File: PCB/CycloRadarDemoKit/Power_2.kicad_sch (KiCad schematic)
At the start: 16 parts, among them U401 AP63203WU, U404 TPS2121RUXR

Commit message: PCB, 3Dmodel
mockup PCB version done, schcematic exported to latex, 3D model generated and exported to latex
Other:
- title: Safety Ride Radar Sensor -> Radar Safety Sensor
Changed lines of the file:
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@@
   (paper "A4")
   (title_block
-    (title "Safety Ride Radar Sensor")
-    (date "2023-12-19")
-    (rev "Rev.: WIP")
+    (title "Radar Safety Sensor")
+    (date "2023-12-20")
+    (rev "Rev.: 1")
     (company "ALPS Electric Czech, s.r.o.")
     (comment 1 "Designed by Martin Tavoda")

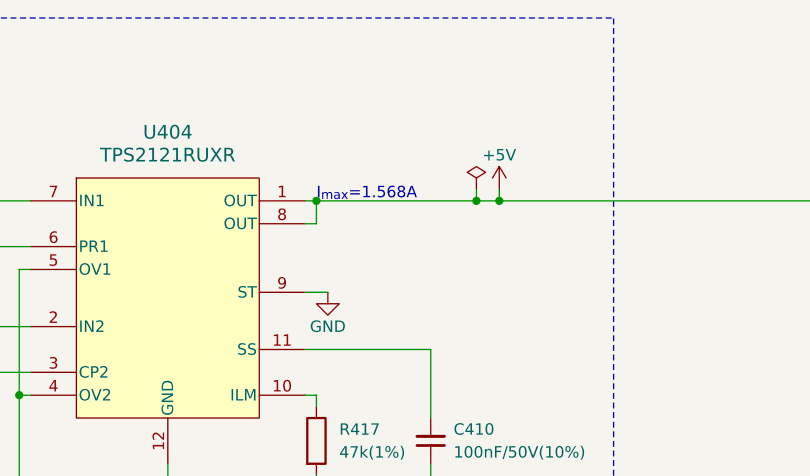
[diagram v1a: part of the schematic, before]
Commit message: sortingAbbr, cosmetics schematic, export schematic to thesis
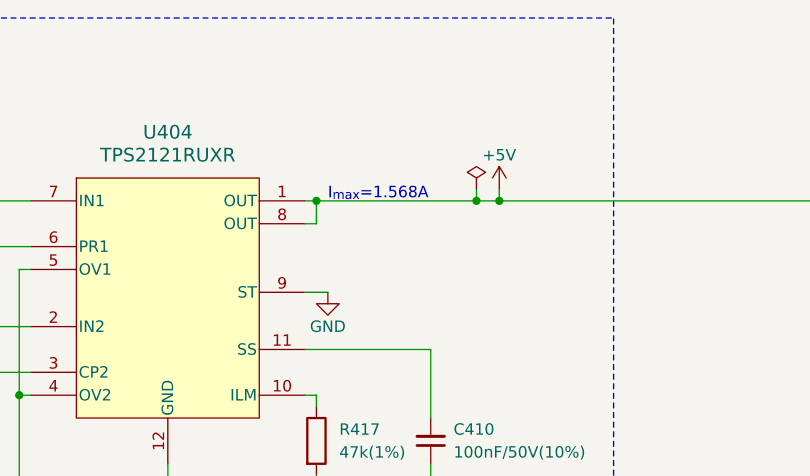
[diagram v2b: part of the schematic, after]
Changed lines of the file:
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@@
     (title "Radar Safety Sensor")
     (date "2023-12-20")
-    (rev "Rev.: 1")
+    (rev "Rev.: 1.0")
     (company "ALPS Electric Czech, s.r.o.")
     (comment 1 "Designed by Martin Tavoda")
@@
     (effects (font (size 2 2) (thickness 0.4) bold) (justify left bottom))
   )
-  (text "I_{max}=1.568A" (at 105.41 57.15 0)
-    (effects (font (size 1.27 1.27)) (justify left bottom))
-  )
+  (text "I_{max}=1.568A" (at 106.68 57.15 0)
+    (effects (font (size 1.27 1.27)) (justify left bottom))
+  )

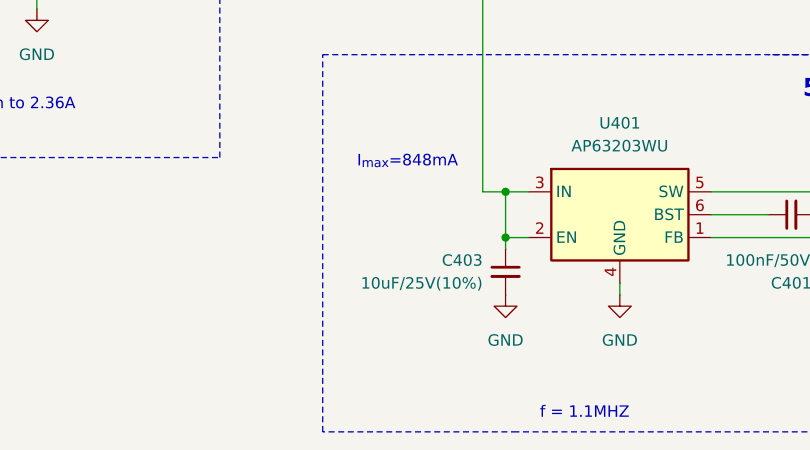
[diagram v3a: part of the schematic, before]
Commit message: Parts ordered on PCB, 1206->0803 10uF, 0803->0402 1uF
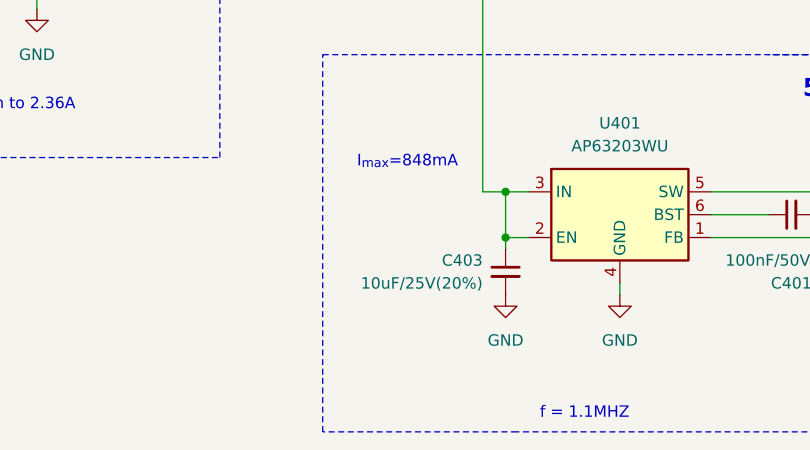
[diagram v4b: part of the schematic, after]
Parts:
- C403: value 10uF/25V(10%) -> 10uF/25V(20%); footprint Capacitor_SMD:C_1206_3216Metric -> Capacitor_SMD:C_0603_1608Metric; LCSC C77090 -> C96446
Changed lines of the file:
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@@
       (effects (font (size 1.27 1.27)) (justify left))
     )
-    (property "Value" "10uF/25V(10%)" (at 167.64 121.9263 0)
+    (property "Value" "10uF/25V(20%)" (at 167.64 121.9263 0)
       (effects (font (size 1.27 1.27)) (justify left))
     )
-    (property "Footprint" "Capacitor_SMD:C_1206_3216Metric" (at 170.18 120.65 0)
+    (property "Footprint" "Capacitor_SMD:C_0603_1608Metric" (at 170.18 120.65 0)
       (effects (font (size 1.27 1.27)) hide)
     )
@@
       (effects (font (size 1.27 1.27)) hide)
     )
-    (property "LCSC" "C77090" (at 170.18 120.65 0)
+    (property "LCSC" "C96446" (at 170.18 120.65 0)
       (effects (font (size 1.27 1.27)) hide)
     )

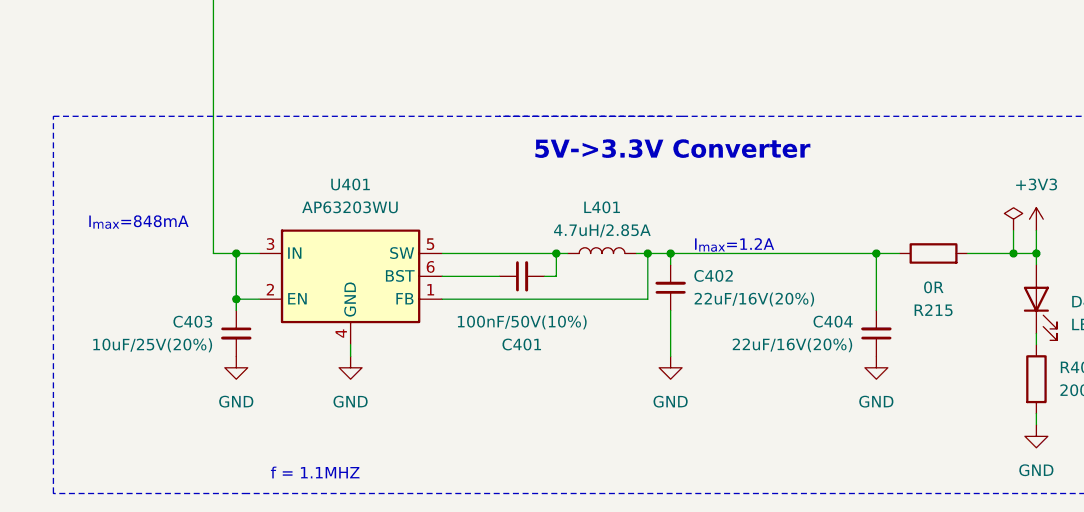
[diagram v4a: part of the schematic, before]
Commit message: DC/DC routed, stuckup properties changed
ready for PCB resize
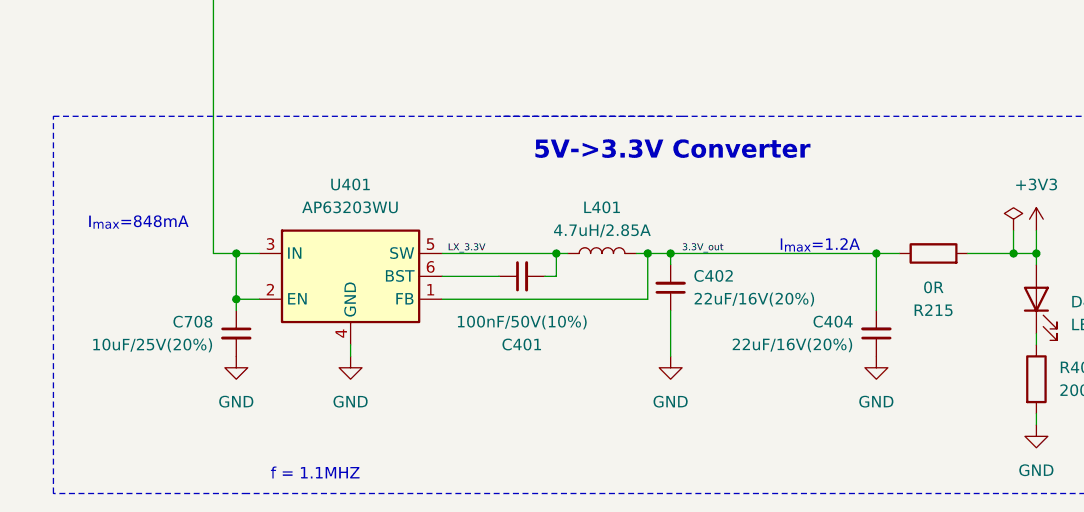
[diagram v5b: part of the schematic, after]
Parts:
- removed C403: 10uF/25V(20%), Capacitor_SMD:C_0603_1608Metric, symbol Device:C_Small
- added C708: 10uF/25V(20%), Capacitor_SMD:C_1206_3216Metric, symbol Device:C_Small
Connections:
- net +5V: now also C708.1
- net GND: now also C708.2
- net 3.3V_out: now reaches C402.2, C404.2, L401.2, R215.1, U401.1 (FB)
- net LX_3.3V: now reaches C401.2, L401.1, U401.5 (SW)
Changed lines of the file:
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@@
+    (stroke (width 0) (type default))
+  )
+  (wire (pts (xy 118.11 91.44) (xy 118.11 86.36))
+    (stroke (width 0) (type default))
+  )
+  (wire (pts (xy 105.41 57.15) (xy 105.41 59.69))
+    (stroke (width 0) (type default))
+  )
+  (wire (pts (xy 218.44 111.76) (xy 215.9 111.76))
+    (stroke (width 0) (type default))
+  )
+  (wire (pts (xy 218.44 111.76) (xy 241.3 111.76))
+    (stroke (width 0) (type default))
+  )
+  (polyline (pts (xy 138.43 107.95) (xy 138.43 36.83))
+    (stroke (width 0) (type dash))
+  )
+  (wire (pts (xy 259.08 111.76) (xy 256.54 111.76))
+    (stroke (width 0) (type default))
+  )
+  (polyline (pts (xy 273.05 138.43) (xy 171.45 138.43))
+    (stroke (width 0) (type dash))
+  )
+  (wire (pts (xy 59.69 62.23) (xy 73.66 62.23))
+    (stroke (width 0) (type default))
+  )
+  (wire (pts (xy 105.41 80.01) (xy 105.41 78.74))
+    (stroke (width 0) (type default))
+  )
+  (wire (pts (xy 215.9 111.76) (xy 214.63 111.76))
+    (stroke (width 0) (type default))
+  )
+  (wire (pts (xy 215.9 116.84) (xy 215.9 111.76))
+    (stroke (width 0) (type default))
+  )
+  (polyline (pts (xy 273.05 96.52) (xy 273.05 138.43))
+    (stroke (width 0) (type dash))
+  )
+  (wire (pts (xy 182.88 123.19) (xy 182.88 121.92))
+    (stroke (width 0) (type default))
+  )
+  (wire (pts (xy 218.44 123.19) (xy 218.44 118.11))
+    (stroke (width 0) (type default))
+  )
+  (wire (pts (xy 72.39 64.77) (xy 72.39 78.74))
     (stroke (width 0) (type default))
   )
   (wire (pts (xy 193.04 111.76) (xy 205.74 111.76))
-    (stroke (width 0) (type default))
-  )
-  (wire (pts (xy 118.11 91.44) (xy 118.11 86.36))
-    (stroke (width 0) (type default))
-  )
-  (wire (pts (xy 105.41 57.15) (xy 105.41 59.69))
-    (stroke (width 0) (type default))
-  )
-  (wire (pts (xy 218.44 111.76) (xy 215.9 111.76))
-    (stroke (width 0) (type default))
-  )
-  (wire (pts (xy 218.44 111.76) (xy 241.3 111.76))
-    (stroke (width 0) (type default))
-  )
-  (polyline (pts (xy 138.43 107.95) (xy 138.43 36.83))
-    (stroke (width 0) (type dash))
-  )
-  (wire (pts (xy 259.08 111.76) (xy 256.54 111.76))
-    (stroke (width 0) (type default))
-  )
-  (polyline (pts (xy 273.05 138.43) (xy 171.45 138.43))
-    (stroke (width 0) (type dash))
-  )
-  (wire (pts (xy 59.69 62.23) (xy 73.66 62.23))
-    (stroke (width 0) (type default))
-  )
-  (wire (pts (xy 105.41 80.01) (xy 105.41 78.74))
-    (stroke (width 0) (type default))
-  )
-  (wire (pts (xy 215.9 111.76) (xy 214.63 111.76))
-    (stroke (width 0) (type default))
-  )
-  (wire (pts (xy 215.9 116.84) (xy 215.9 111.76))
-    (stroke (width 0) (type default))
-  )
-  (polyline (pts (xy 273.05 96.52) (xy 273.05 138.43))
-    (stroke (width 0) (type dash))
-  )
-  (wire (pts (xy 182.88 123.19) (xy 182.88 121.92))
-    (stroke (width 0) (type default))
-  )
-  (wire (pts (xy 218.44 123.19) (xy 218.44 118.11))
-    (stroke (width 0) (type default))
-  )
-  (wire (pts (xy 72.39 64.77) (xy 72.39 78.74))
     (stroke (width 0) (type default))
   )
@@
     (effects (font (size 1.27 1.27)) (justify left bottom))
   )
-  (text "I_{max}=1.2A" (at 220.98 111.76 0)
+  (text "I_{max}=1.2A" (at 230.505 111.76 0)
     (effects (font (size 1.27 1.27)) (justify left bottom))
   )
@@
     (effects (font (size 1.27 1.27)) (justify left bottom))
   )
+  (label "3.3V_out" (at 219.71 111.76 0) (fields_autoplaced)
+    (effects (font (size 0.762 0.762)) (justify left bottom))
+  )
+  (label "LX_3.3V" (at 193.675 111.76 0) (fields_autoplaced)
+    (effects (font (size 0.762 0.762)) (justify left bottom))
+  )
   (hierarchical_label "Battery 5V" (shape input) (at 46.99 57.15 180) (fields_autoplaced)
     (effects (font (size 1.27 1.27)) (justify right))
@@
   (symbol (lib_id "Device:C_Small") (at 170.18 120.65 0) (mirror y) (unit 1)
     (in_bom yes) (on_board yes) (dnp no)
-    (property "Reference" "C403" (at 167.64 119.3863 0)
+    (property "Reference" "C708" (at 167.64 119.3863 0)
       (effects (font (size 1.27 1.27)) (justify left))
     )
@@
       (effects (font (size 1.27 1.27)) (justify left))
     )
-    (property "Footprint" "Capacitor_SMD:C_0603_1608Metric" (at 170.18 120.65 0)
+    (property "Footprint" "Capacitor_SMD:C_1206_3216Metric" (at 170.18 120.65 0)
       (effects (font (size 1.27 1.27)) hide)
     )
@@
       (effects (font (size 1.27 1.27)) hide)
     )
-    (property "LCSC" "C96446" (at 170.18 120.65 0)
-      (effects (font (size 1.27 1.27)) hide)
-    )
-    (pin "2")
-    (pin "1")
-    (instances
-      (project "CycloRadarDemoKit"
-        (path "/c2cd7ca4-4652-4b3d-a3a8-1cfa66cb11e9/8e86b850-15ce-40c4-bda7-5d0afa1e377d"
-          (reference "C403") (unit 1)
+    (property "LCSC" "C13585" (at 170.18 120.65 0)
+      (effects (font (size 1.27 1.27)) hide)
+    )
+    (pin "2")
+    (pin "1")
+    (instances
+      (project "CycloRadarDemoKit"
+        (path "/c2cd7ca4-4652-4b3d-a3a8-1cfa66cb11e9/8e86b850-15ce-40c4-bda7-5d0afa1e377d"
+          (reference "C708") (unit 1)
         )
         (path "/c2cd7ca4-4652-4b3d-a3a8-1cfa66cb11e9/724c5e61-df30-4d89-bd6d-7121cc967a43"
@@
       (effects (font (size 1.27 1.27) italic) hide)
     )
-    (property "Datasheet" "TPS2121RUXR" (at 88.9 68.58 0)
+    (property "Datasheet" "https://www.ti.com/lit/ds/symlink/tps2120.pdf?ts=1705780527987&ref_url=https%253A%252F%252Fwww.google.com%252F" (at 88.9 68.58 0)
       (effects (font (size 1.27 1.27) italic) hide)
     )

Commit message: start of repair after review
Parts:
- C708: value 10uF/25V(20%) -> 10uF/50V(20%)
- R215: now left out of the parts list
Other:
- note added: "I_{max}=1.28A"
- note removed: "I_{max}=1.568A"
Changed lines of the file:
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@@
     (effects (font (size 2 2) (thickness 0.4) bold) (justify left bottom))
   )
-  (text "I_{max}=1.568A" (at 106.68 57.15 0)
+  (text "I_{max}=1.28A" (at 106.68 57.15 0)
     (effects (font (size 1.27 1.27)) (justify left bottom))
   )
@@
       (effects (font (size 1.27 1.27)) (justify left))
     )
-    (property "Value" "10uF/25V(20%)" (at 167.64 121.9263 0)
+    (property "Value" "10uF/50V(20%)" (at 167.64 121.9263 0)
       (effects (font (size 1.27 1.27)) (justify left))
     )
@@
   )
   (symbol (lib_id "Device:R") (at 50.8 82.55 180) (unit 1)
-    (in_bom yes) (on_board yes) (dnp yes) (fields_autoplaced)
+    (in_bom no) (on_board yes) (dnp yes) (fields_autoplaced)
     (property "Reference" "R215" (at 53.34 81.28 0)
       (effects (font (size 1.27 1.27)) (justify right))

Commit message: JLCPCB mistakes repaired, cosmetics on PCB
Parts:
- C402, C404: LCSC C87162 -> C12891
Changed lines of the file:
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@@
       (effects (font (size 1.27 1.27)) hide)
     )
-    (property "LCSC" "C87162" (at 218.44 115.57 0)
+    (property "LCSC" "C12891" (at 218.44 115.57 0)
       (effects (font (size 1.27 1.27)) hide)
     )
@@
       (effects (font (size 1.27 1.27)) hide)
     )
-    (property "LCSC" "C87162" (at 241.3 120.65 0)
-      (effects (font (size 1.27 1.27)) hide)
-    )
+    (property "LCSC" "C12891" (at 241.3 120.65 0)
+      (effects (font (size 1.27 1.27)) hide)
+    )

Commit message: Sematic Versioning implemented, whish list added
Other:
- company: ALPS Electric Czech, s.r.o. -> ${COMPANY}
- title: Radar Safety Sensor -> ${TITLE}
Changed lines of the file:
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@@
   (paper "A4")
   (title_block
-    (title "Radar Safety Sensor")
-    (date "2023-12-20")
-    (rev "Rev.: 1.0")
-    (company "ALPS Electric Czech, s.r.o.")
-    (comment 1 "Designed by Martin Tavoda")
+    (title "${TITLE}")
+    (date "${DATE}")
+    (rev "${REVISION}")
+    (company "${COMPANY}")
+    (comment 1 "${CREATOR}")
+    (comment 2 "${APPROVER}")
+    (comment 3 "${STATUS}")
+    (comment 4 "${LANG}")
+    (comment 5 "${NOTE}")
   )
   (junction (at 215.9 111.76) (diameter 0) (color 0 0 0 0)
